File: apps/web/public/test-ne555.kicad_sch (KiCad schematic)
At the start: 9 parts, among them J1 PWR_5V, U1 NE555P

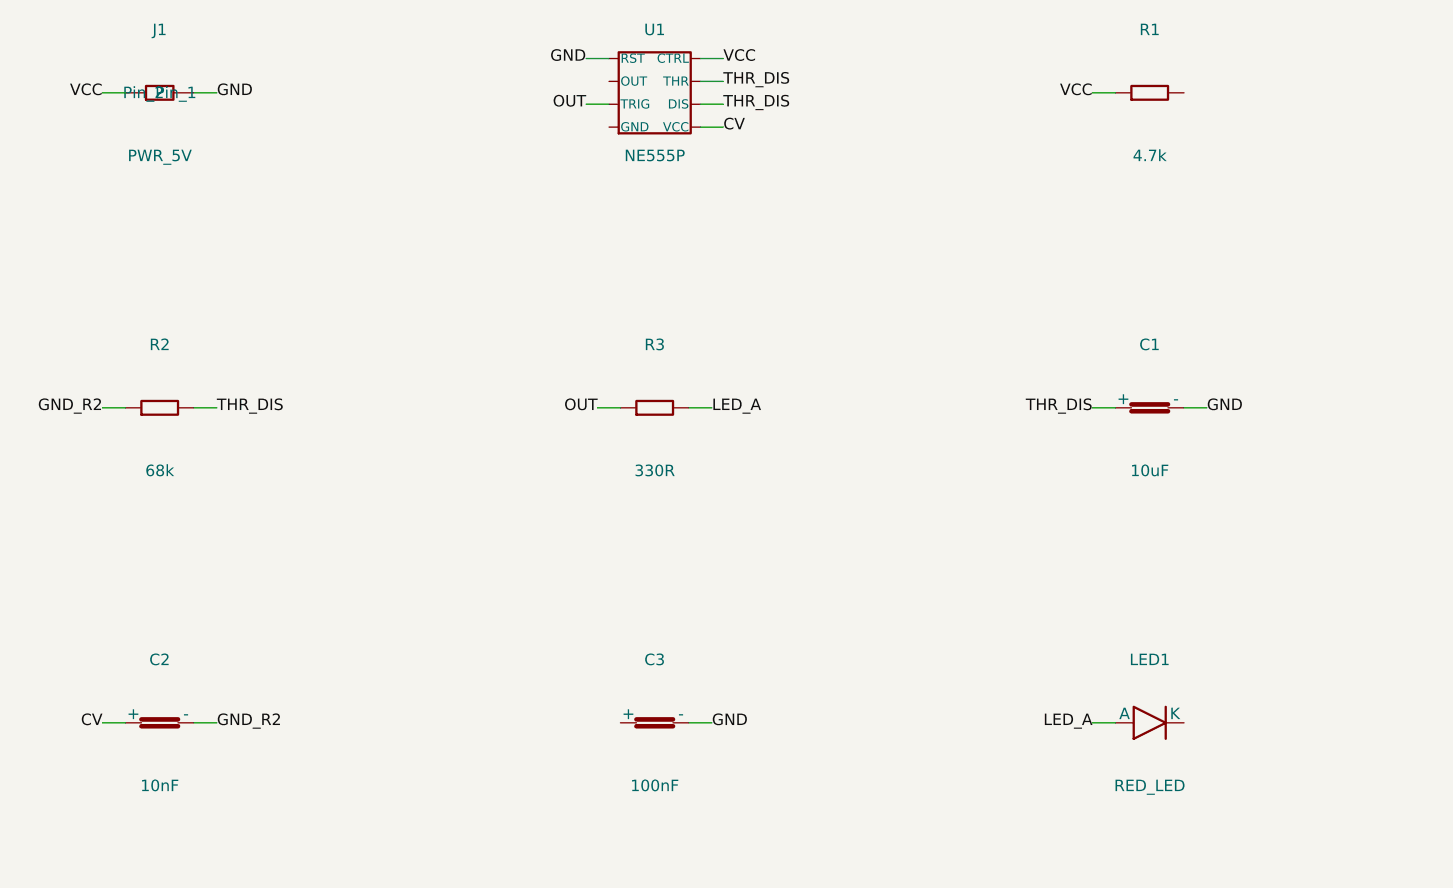
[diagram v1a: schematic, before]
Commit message: fix(viewer): correct title block detection and paper height formula
- JS: TITLE_HEIGHT=43mm (fixed KiCad value, not 30% ratio) + dual-constraint
  cy = min(maxCy_frame, maxCy_title) guarantees frame visible + title hidden
- JS: waitAndZoom triggers on symbols OR net_labels (handles no-label schematics)
- Python: paper_h = component_bottom_y + 6mm gap + 44mm title block (replaces
  broken TITLE_RATIO=0.30 formula that left zero gap before title block)
- Regenerated test schematics: LM7805 (115mm), NE555 (150mm), ESP32 (150mm)
- Verified all 3 tabs: frame visible, all components shown, title block hidden
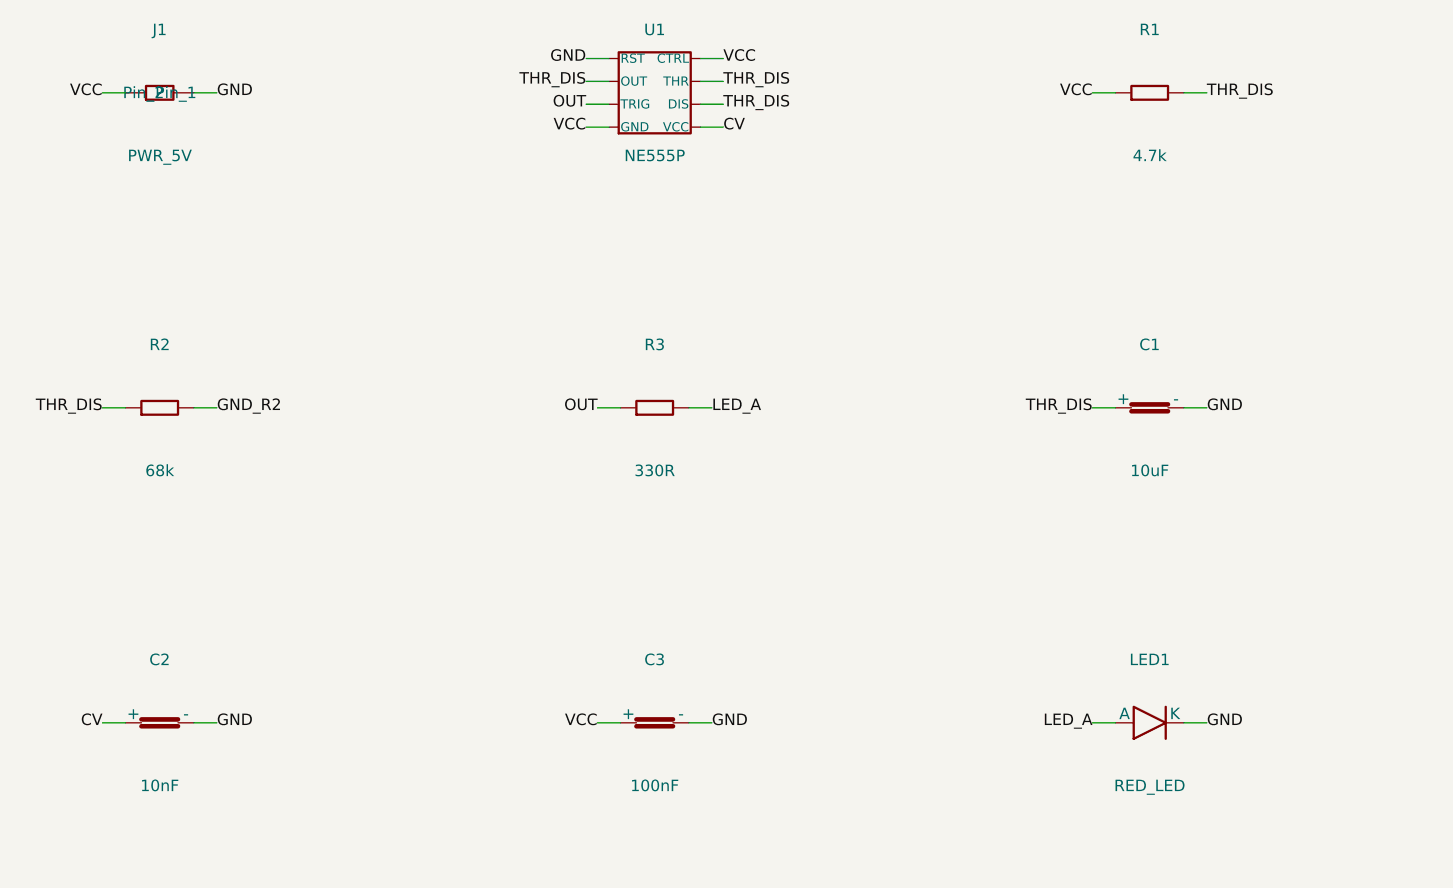
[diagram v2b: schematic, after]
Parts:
- C1: footprint Capacitor_THT:C_Radial_D5.0mm_H11.0mm_P2.00mm -> Capacitor_SMD:C_1206_3216Metric
- C2, C3: footprint Capacitor_THT:C_Disc_D5.0mm_W2.5mm_P5.00mm -> Capacitor_SMD:C_0603_1608Metric
- LED1: footprint LED_THT:LED_D5.0mm -> LED_SMD:LED_0603_1608Metric
- R1, R2, R3: footprint Resistor_THT:R_Axial_DIN0207_L6.3mm_D2.5mm_P10.16mm_Horizontal -> Resistor_SMD:R_0603_1608Metric
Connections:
- net GND: now also C2.2 (-), LED1.2 (K)
- net GND_R2: now also R2.2; no longer C2.2 (-), R2.1
- net THR_DIS: now also R1.2, R2.1, U1.3 (OUT); no longer R2.2
- net VCC: now also C3.1 (+), U1.1 (GND)
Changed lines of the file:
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@@
 (kicad_sch (version 20230121) (generator "layrix-circuit-synth")
-  (paper "User" 149 143)
+  (paper "User" 149 150)
   (symbol (lib_id "Connector_Generic:Conn_01x02") (at 12 12 0) (unit 1) (in_bom yes) (on_board yes)
     (property "Reference" "J1" (at 12 5 0) (effects (font (size 1.27 1.27)) (justify center)))
@@
     (property "Reference" "R1" (at 122 5 0) (effects (font (size 1.27 1.27)) (justify center)))
     (property "Value" "4.7k" (at 122 19 0) (effects (font (size 1.27 1.27)) (justify center)))
-    (property "Footprint" "Resistor_THT:R_Axial_DIN0207_L6.3mm_D2.5mm_P10.16mm_Horizontal" (at 122 22 0) (effects (font (size 1.27 1.27)) (hide yes)))
+    (property "Footprint" "Resistor_SMD:R_0603_1608Metric" (at 122 22 0) (effects (font (size 1.27 1.27)) (hide yes)))
   )
   (symbol (lib_id "Device:R") (at 12 47 0) (unit 1) (in_bom yes) (on_board yes)
     (property "Reference" "R2" (at 12 40 0) (effects (font (size 1.27 1.27)) (justify center)))
     (property "Value" "68k" (at 12 54 0) (effects (font (size 1.27 1.27)) (justify center)))
-    (property "Footprint" "Resistor_THT:R_Axial_DIN0207_L6.3mm_D2.5mm_P10.16mm_Horizontal" (at 12 57 0) (effects (font (size 1.27 1.27)) (hide yes)))
+    (property "Footprint" "Resistor_SMD:R_0603_1608Metric" (at 12 57 0) (effects (font (size 1.27 1.27)) (hide yes)))
   )
   (symbol (lib_id "Device:R") (at 67 47 0) (unit 1) (in_bom yes) (on_board yes)
     (property "Reference" "R3" (at 67 40 0) (effects (font (size 1.27 1.27)) (justify center)))
     (property "Value" "330R" (at 67 54 0) (effects (font (size 1.27 1.27)) (justify center)))
-    (property "Footprint" "Resistor_THT:R_Axial_DIN0207_L6.3mm_D2.5mm_P10.16mm_Horizontal" (at 67 57 0) (effects (font (size 1.27 1.27)) (hide yes)))
+    (property "Footprint" "Resistor_SMD:R_0603_1608Metric" (at 67 57 0) (effects (font (size 1.27 1.27)) (hide yes)))
   )
   (symbol (lib_id "Device:C") (at 122 47 0) (unit 1) (in_bom yes) (on_board yes)
     (property "Reference" "C1" (at 122 40 0) (effects (font (size 1.27 1.27)) (justify center)))
     (property "Value" "10uF" (at 122 54 0) (effects (font (size 1.27 1.27)) (justify center)))
-    (property "Footprint" "Capacitor_THT:C_Radial_D5.0mm_H11.0mm_P2.00mm" (at 122 57 0) (effects (font (size 1.27 1.27)) (hide yes)))
+    (property "Footprint" "Capacitor_SMD:C_1206_3216Metric" (at 122 57 0) (effects (font (size 1.27 1.27)) (hide yes)))
   )
   (symbol (lib_id "Device:C") (at 12 82 0) (unit 1) (in_bom yes) (on_board yes)
     (property "Reference" "C2" (at 12 75 0) (effects (font (size 1.27 1.27)) (justify center)))
     (property "Value" "10nF" (at 12 89 0) (effects (font (size 1.27 1.27)) (justify center)))
-    (property "Footprint" "Capacitor_THT:C_Disc_D5.0mm_W2.5mm_P5.00mm" (at 12 92 0) (effects (font (size 1.27 1.27)) (hide yes)))
+    (property "Footprint" "Capacitor_SMD:C_0603_1608Metric" (at 12 92 0) (effects (font (size 1.27 1.27)) (hide yes)))
   )
   (symbol (lib_id "Device:C") (at 67 82 0) (unit 1) (in_bom yes) (on_board yes)
     (property "Reference" "C3" (at 67 75 0) (effects (font (size 1.27 1.27)) (justify center)))
     (property "Value" "100nF" (at 67 89 0) (effects (font (size 1.27 1.27)) (justify center)))
-    (property "Footprint" "Capacitor_THT:C_Disc_D5.0mm_W2.5mm_P5.00mm" (at 67 92 0) (effects (font (size 1.27 1.27)) (hide yes)))
+    (property "Footprint" "Capacitor_SMD:C_0603_1608Metric" (at 67 92 0) (effects (font (size 1.27 1.27)) (hide yes)))
   )
   (symbol (lib_id "Device:LED") (at 122 82 0) (unit 1) (in_bom yes) (on_board yes)
     (property "Reference" "LED1" (at 122 75 0) (effects (font (size 1.27 1.27)) (justify center)))
     (property "Value" "RED_LED" (at 122 89 0) (effects (font (size 1.27 1.27)) (justify center)))
-    (property "Footprint" "LED_THT:LED_D5.0mm" (at 122 92 0) (effects (font (size 1.27 1.27)) (hide yes)))
+    (property "Footprint" "LED_SMD:LED_0603_1608Metric" (at 122 92 0) (effects (font (size 1.27 1.27)) (hide yes)))
   )
-  (wire (pts (xy 8.19 12.0) (xy 5.65 12.0)) (stroke (width 0.1524) (type default)))
-  (label "VCC" (at 5.65 12.0 180) (effects (font (size 1.27 1.27))))
-  (wire (pts (xy 72.08 8.19) (xy 74.62 8.19)) (stroke (width 0.1524) (type default)))
-  (label "VCC" (at 74.62 8.19 0) (effects (font (size 1.27 1.27))))
-  (wire (pts (xy 118.19 12.0) (xy 115.65 12.0)) (stroke (width 0.1524) (type default)))
-  (label "VCC" (at 115.65 12.0 180) (effects (font (size 1.27 1.27))))
   (wire (pts (xy 15.81 12.0) (xy 18.35 12.0)) (stroke (width 0.1524) (type default)))
   (label "GND" (at 18.35 12.0 0) (effects (font (size 1.27 1.27))))
@@
   (wire (pts (xy 125.81 47.0) (xy 128.35 47.0)) (stroke (width 0.1524) (type default)))
   (label "GND" (at 128.35 47.0 0) (effects (font (size 1.27 1.27))))
+  (wire (pts (xy 15.81 82.0) (xy 18.35 82.0)) (stroke (width 0.1524) (type default)))
+  (label "GND" (at 18.35 82.0 0) (effects (font (size 1.27 1.27))))
   (wire (pts (xy 70.81 82.0) (xy 73.35 82.0)) (stroke (width 0.1524) (type default)))
   (label "GND" (at 73.35 82.0 0) (effects (font (size 1.27 1.27))))
-  (wire (pts (xy 72.08 13.27) (xy 74.62 13.27)) (stroke (width 0.1524) (type default)))
-  (label "THR_DIS" (at 74.62 13.27 0) (effects (font (size 1.27 1.27))))
-  (wire (pts (xy 72.08 10.73) (xy 74.62 10.73)) (stroke (width 0.1524) (type default)))
-  (label "THR_DIS" (at 74.62 10.73 0) (effects (font (size 1.27 1.27))))
-  (wire (pts (xy 15.81 47.0) (xy 18.35 47.0)) (stroke (width 0.1524) (type default)))
-  (label "THR_DIS" (at 18.35 47.0 0) (effects (font (size 1.27 1.27))))
-  (wire (pts (xy 118.19 47.0) (xy 115.65 47.0)) (stroke (width 0.1524) (type default)))
-  (label "THR_DIS" (at 115.65 47.0 180) (effects (font (size 1.27 1.27))))
+  (wire (pts (xy 125.81 82.0) (xy 128.35 82.0)) (stroke (width 0.1524) (type default)))
+  (label "GND" (at 128.35 82.0 0) (effects (font (size 1.27 1.27))))
+  (wire (pts (xy 8.19 12.0) (xy 5.65 12.0)) (stroke (width 0.1524) (type default)))
+  (label "VCC" (at 5.65 12.0 180) (effects (font (size 1.27 1.27))))
+  (wire (pts (xy 72.08 8.19) (xy 74.62 8.19)) (stroke (width 0.1524) (type default)))
+  (label "VCC" (at 74.62 8.19 0) (effects (font (size 1.27 1.27))))
+  (wire (pts (xy 61.92 15.81) (xy 59.38 15.81)) (stroke (width 0.1524) (type default)))
+  (label "VCC" (at 59.38 15.81 180) (effects (font (size 1.27 1.27))))
+  (wire (pts (xy 118.19 12.0) (xy 115.65 12.0)) (stroke (width 0.1524) (type default)))
+  (label "VCC" (at 115.65 12.0 180) (effects (font (size 1.27 1.27))))
+  (wire (pts (xy 63.19 82.0) (xy 60.65 82.0)) (stroke (width 0.1524) (type default)))
+  (label "VCC" (at 60.65 82.0 180) (effects (font (size 1.27 1.27))))
   (wire (pts (xy 61.92 13.27) (xy 59.38 13.27)) (stroke (width 0.1524) (type default)))
   (label "OUT" (at 59.38 13.27 180) (effects (font (size 1.27 1.27))))
@@
   (wire (pts (xy 118.19 82.0) (xy 115.65 82.0)) (stroke (width 0.1524) (type default)))
   (label "LED_A" (at 115.65 82.0 180) (effects (font (size 1.27 1.27))))
+  (wire (pts (xy 125.81 12.0) (xy 128.35 12.0)) (stroke (width 0.1524) (type default)))
+  (label "THR_DIS" (at 128.35 12.0 0) (effects (font (size 1.27 1.27))))
+  (wire (pts (xy 8.19 47.0) (xy 5.65 47.0)) (stroke (width 0.1524) (type default)))
+  (label "THR_DIS" (at 5.65 47.0 180) (effects (font (size 1.27 1.27))))
+  (wire (pts (xy 61.92 10.73) (xy 59.38 10.73)) (stroke (width 0.1524) (type default)))
+  (label "THR_DIS" (at 59.38 10.73 180) (effects (font (size 1.27 1.27))))
+  (wire (pts (xy 72.08 13.27) (xy 74.62 13.27)) (stroke (width 0.1524) (type default)))
+  (label "THR_DIS" (at 74.62 13.27 0) (effects (font (size 1.27 1.27))))
+  (wire (pts (xy 72.08 10.73) (xy 74.62 10.73)) (stroke (width 0.1524) (type default)))
+  (label "THR_DIS" (at 74.62 10.73 0) (effects (font (size 1.27 1.27))))
+  (wire (pts (xy 118.19 47.0) (xy 115.65 47.0)) (stroke (width 0.1524) (type default)))
+  (label "THR_DIS" (at 115.65 47.0 180) (effects (font (size 1.27 1.27))))
+  (wire (pts (xy 15.81 47.0) (xy 18.35 47.0)) (stroke (width 0.1524) (type default)))
+  (label "GND_R2" (at 18.35 47.0 0) (effects (font (size 1.27 1.27))))
   (wire (pts (xy 72.08 15.81) (xy 74.62 15.81)) (stroke (width 0.1524) (type default)))
   (label "CV" (at 74.62 15.81 0) (effects (font (size 1.27 1.27))))
   (wire (pts (xy 8.19 82.0) (xy 5.65 82.0)) (stroke (width 0.1524) (type default)))
   (label "CV" (at 5.65 82.0 180) (effects (font (size 1.27 1.27))))
-  (wire (pts (xy 8.19 47.0) (xy 5.65 47.0)) (stroke (width 0.1524) (type default)))
-  (label "GND_R2" (at 5.65 47.0 180) (effects (font (size 1.27 1.27))))
-  (wire (pts (xy 15.81 82.0) (xy 18.35 82.0)) (stroke (width 0.1524) (type default)))
-  (label "GND_R2" (at 18.35 82.0 0) (effects (font (size 1.27 1.27))))
   (sheet_instances (path "/" (page "1")))
 )

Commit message: fix(layout): margin_top 12→20mm — composants 15mm du bord cadre interne
Composants étaient à y=12mm (7mm du bord interne), visuellement collés au cadre.
Maintenant à y=20mm (15mm de marge), clairement à l'intérieur du cadre.

- circuit_synth.py: margin_top = 20mm
- test-lm7805.kicad_sch: paper 149x123 (was 115)
- test-ne555.kicad_sch: paper 149x158 (was 150)
- test-esp32.kicad_sch: paper 149x158 (was 150)
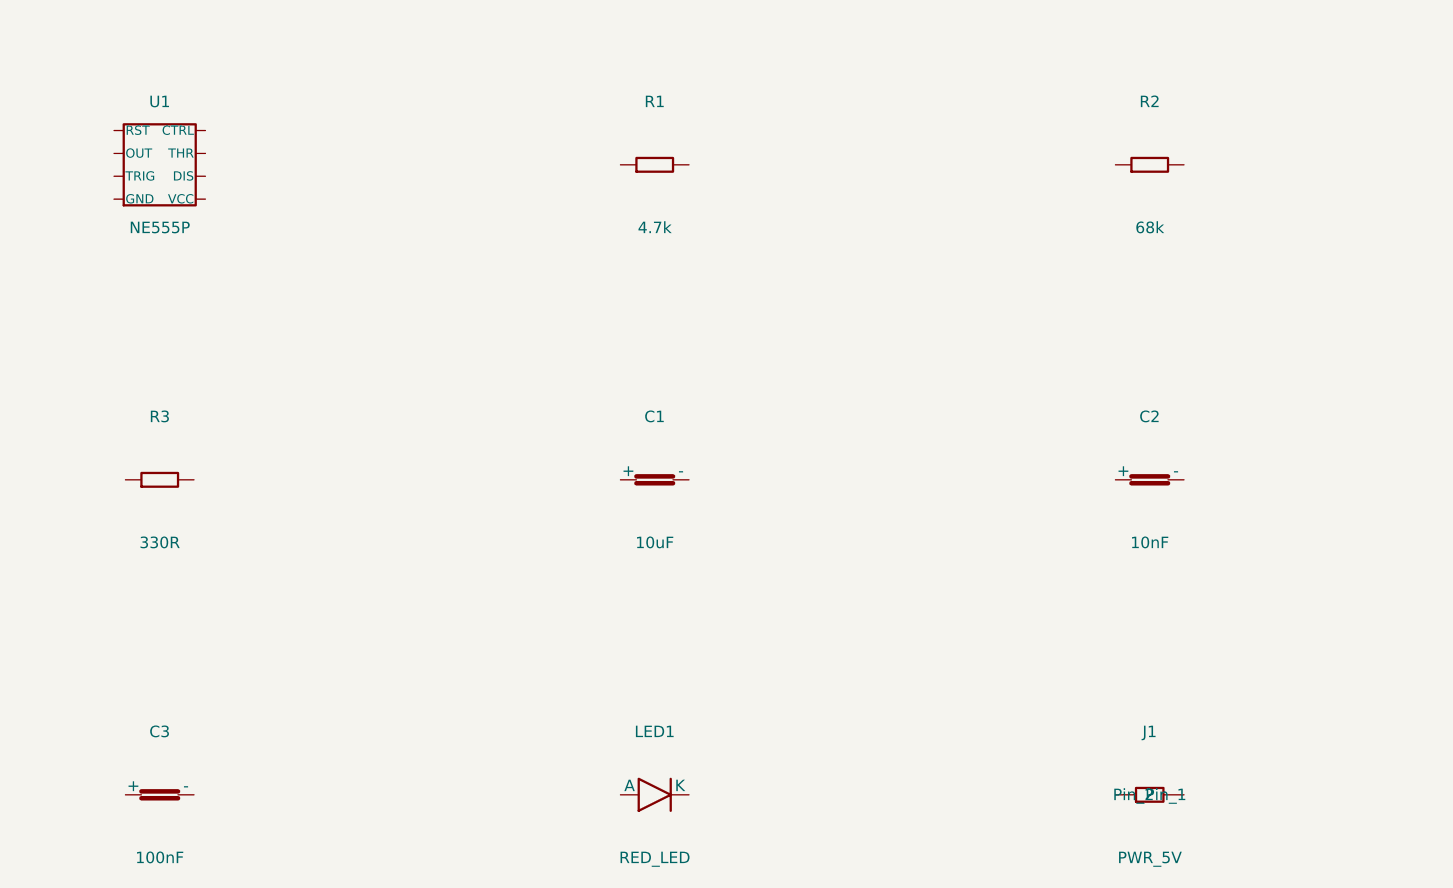
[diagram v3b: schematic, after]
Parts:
- C1: footprint Capacitor_SMD:C_1206_3216Metric -> Capacitor_THT:C_Disc_D5.0mm_W2.5mm_P5.00mm
- C2, C3: footprint Capacitor_SMD:C_0603_1608Metric -> Capacitor_THT:C_Disc_D5.0mm_W2.5mm_P5.00mm
- LED1: footprint LED_SMD:LED_0603_1608Metric -> LED_THT:LED_D5.0mm
- R1, R2, R3: footprint Resistor_SMD:R_0603_1608Metric -> Resistor_THT:R_Axial_DIN0207_L6.3mm_D2.5mm_P10.16mm_Horizontal
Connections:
- net CV: no longer names the net of C2.1 (+)
- net CV: no longer U1.8 (VCC)
- removed net GND: C1.2 (-), C2.2 (-), C3.2 (-), J1.2 (Pin_2), LED1.2 (K), U1.4 (RST)
- net GND_R2: no longer names the net of R2.2
- net LED_A: no longer names the net of R3.2
- net LED_A: no longer LED1.1 (A)
- net OUT: no longer names the net of R3.1
- net OUT: no longer U1.2 (TRIG)
- removed net THR_DIS: C1.1 (+), R1.2, R2.1, U1.3 (OUT), U1.6 (THR), U1.7 (DIS)
- removed net VCC: C3.1 (+), J1.1 (Pin_1), R1.1, U1.1 (GND), U1.5 (CTRL)
